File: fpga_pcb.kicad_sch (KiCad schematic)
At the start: 0 parts

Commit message: Aded power and USB
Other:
- added sheet FPGA (FPGA.kicad_sch)
- added sheet Power (Power.kicad_sch)
- added sheet USB (USB.kicad_sch)
- note added: "TLV320ADC6140"
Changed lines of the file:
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@@
 	(generator_version "10.0")
 	(paper "A4")
+	(text "TLV320ADC6140"
+		(exclude_from_sim no)
+		(at 73.152 29.21 0)
+		(effects
+			(font
+				(size 1.27 1.27)
+			)
+		)
+	)
+	(sheet
+		(at 45.72 86.36)
+		(size 43.18 53.34)
+		(exclude_from_sim no)
+		(in_bom yes)
+		(on_board yes)
+		(dnp no)
+		(fields_autoplaced yes)
+		(stroke
+			(width 0.1524)
+			(type solid)
+		)
+		(fill
+			(color 0 0 0 0)
+		)
+		(property "Sheetname" "USB"
+			(at 45.72 85.6484 0)
+			(show_name no)
+			(do_not_autoplace no)
+			(effects
+				(font
+					(size 1.27 1.27)
+				)
+				(justify left bottom)
+			)
+		)
+		(property "Sheetfile" "USB.kicad_sch"
+			(at 45.72 140.2846 0)
+			(show_name no)
+			(do_not_autoplace no)
+			(effects
+				(font
+					(size 1.27 1.27)
+				)
+				(justify left top)
+			)
+		)
+		(pin "FTDI_SPI" bidirectional
+			(at 88.9 93.98 0)
+			(effects
+				(font
+					(size 1.27 1.27)
+				)
+				(justify right)
+			)
+		)
+		(pin "FTDI_BB" bidirectional
+			(at 88.9 105.41 0)
+			(effects
+				(font
+					(size 1.27 1.27)
+				)
+				(justify right)
+			)
+		)
+		(pin "FTDI_JTAG" bidirectional
+			(at 88.9 97.79 0)
+			(effects
+				(font
+					(size 1.27 1.27)
+				)
+				(justify right)
+			)
+		)
+		(pin "FTDI_UART" bidirectional
+			(at 88.9 101.6 0)
+			(effects
+				(font
+					(size 1.27 1.27)
+				)
+				(justify right)
+			)
+		)
+		(instances
+			(project "fpga_pcb"
+				(path "/0e44f7b0-1a4a-4ef8-a122-38b9269be26a"
+					(page "4")
+				)
+			)
+		)
+	)
+	(sheet
+		(at 121.92 85.09)
+		(size 49.53 50.8)
+		(exclude_from_sim no)
+		(in_bom yes)
+		(on_board yes)
+		(dnp no)
+		(fields_autoplaced yes)
+		(stroke
+			(width 0.1524)
+			(type solid)
+		)
+		(fill
+			(color 0 0 0 0)
+		)
+		(property "Sheetname" "FPGA"
+			(at 121.92 84.3784 0)
+			(show_name no)
+			(do_not_autoplace no)
+			(effects
+				(font
+					(size 1.27 1.27)
+				)
+				(justify left bottom)
+			)
+		)
+		(property "Sheetfile" "FPGA.kicad_sch"
+			(at 121.92 136.4746 0)
+			(show_name no)
+			(do_not_autoplace no)
+			(effects
+				(font
+					(size 1.27 1.27)
+				)
+				(justify left top)
+			)
+		)
+		(pin "FTDI_JTAG" bidirectional
+			(at 121.92 104.14 180)
+			(effects
+				(font
+					(size 1.27 1.27)
+				)
+				(justify left)
+			)
+		)
+		(pin "FTDI_SPI" bidirectional
+			(at 121.92 100.33 180)
+			(effects
+				(font
+					(size 1.27 1.27)
+				)
+				(justify left)
+			)
+		)
+		(instances
+			(project "fpga_pcb"
+				(path "/0e44f7b0-1a4a-4ef8-a122-38b9269be26a"
+					(page "2")
+				)
+			)
+		)
+	)
+	(sheet
+		(at 233.68 17.78)
+		(size 33.02 40.64)
+		(exclude_from_sim no)
+		(in_bom yes)
+		(on_board yes)
+		(dnp no)
+		(fields_autoplaced yes)
+		(stroke
+			(width 0.1524)
+			(type solid)
+		)
+		(fill
+			(color 0 0 0 0)
+		)
+		(property "Sheetname" "Power"
+			(at 233.68 17.0684 0)
+			(show_name no)
+			(do_not_autoplace no)
+			(effects
+				(font
+					(size 1.27 1.27)
+				)
+				(justify left bottom)
+			)
+		)
+		(property "Sheetfile" "Power.kicad_sch"
+			(at 233.68 59.0046 0)
+			(show_name no)
+			(do_not_autoplace no)
+			(effects
+				(font
+					(size 1.27 1.27)
+				)
+				(justify left top)
+			)
+		)
+		(instances
+			(project "fpga_pcb"
+				(path "/0e44f7b0-1a4a-4ef8-a122-38b9269be26a"
+					(page "3")
+				)
+			)
+		)
+	)
 	(sheet_instances
 		(path "/"

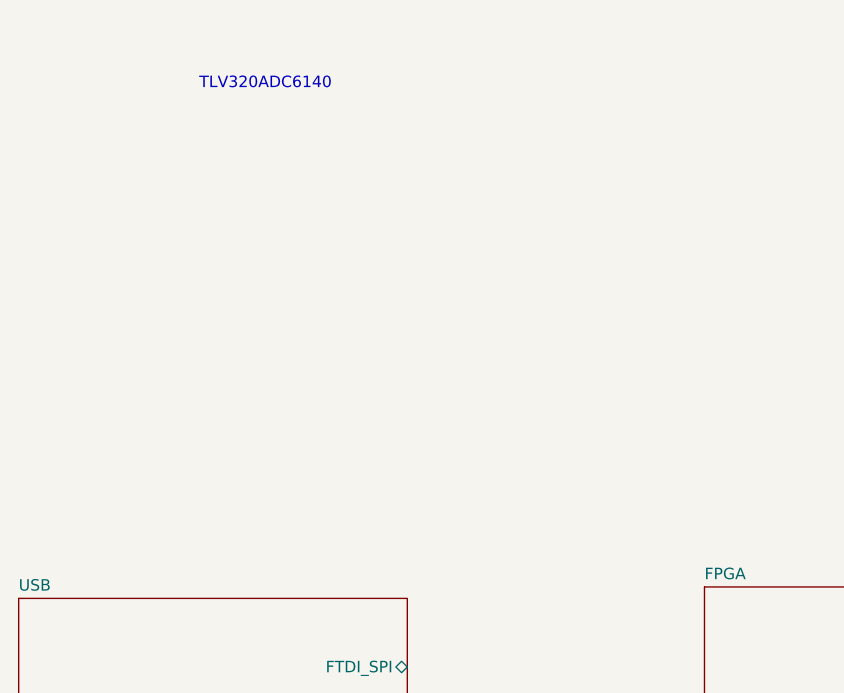
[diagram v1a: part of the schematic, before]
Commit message: Added ADC
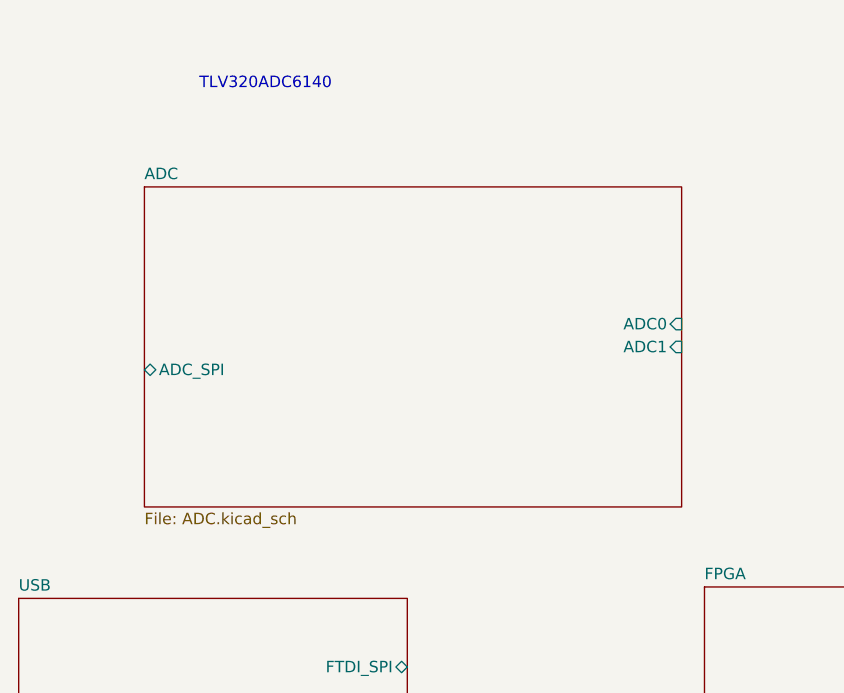
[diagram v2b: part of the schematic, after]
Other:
- added sheet ADC (ADC.kicad_sch)
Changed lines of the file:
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@@
+	)
+	(sheet
+		(at 59.69 40.64)
+		(size 59.69 35.56)
+		(exclude_from_sim no)
+		(in_bom yes)
+		(on_board yes)
+		(dnp no)
+		(fields_autoplaced yes)
+		(stroke
+			(width 0.1524)
+			(type solid)
+		)
+		(fill
+			(color 0 0 0 0)
+		)
+		(property "Sheetname" "ADC"
+			(at 59.69 39.9284 0)
+			(show_name no)
+			(do_not_autoplace no)
+			(effects
+				(font
+					(size 1.27 1.27)
+				)
+				(justify left bottom)
+			)
+		)
+		(property "Sheetfile" "ADC.kicad_sch"
+			(at 59.69 76.7846 0)
+			(show_name no)
+			(do_not_autoplace no)
+			(effects
+				(font
+					(size 1.27 1.27)
+				)
+				(justify left top)
+			)
+		)
+		(pin "ADC0" input
+			(at 119.38 55.88 0)
+			(effects
+				(font
+					(size 1.27 1.27)
+				)
+				(justify right)
+			)
+		)
+		(pin "ADC1" input
+			(at 119.38 58.42 0)
+			(effects
+				(font
+					(size 1.27 1.27)
+				)
+				(justify right)
+			)
+		)
+		(pin "ADC_SPI" bidirectional
+			(at 59.69 60.96 180)
+			(effects
+				(font
+					(size 1.27 1.27)
+				)
+				(justify left)
+			)
+		)
+		(instances
+			(project "fpga_pcb"
+				(path "/0e44f7b0-1a4a-4ef8-a122-38b9269be26a"
+					(page "5")
+				)
+			)
+		)
 	)
 	(sheet

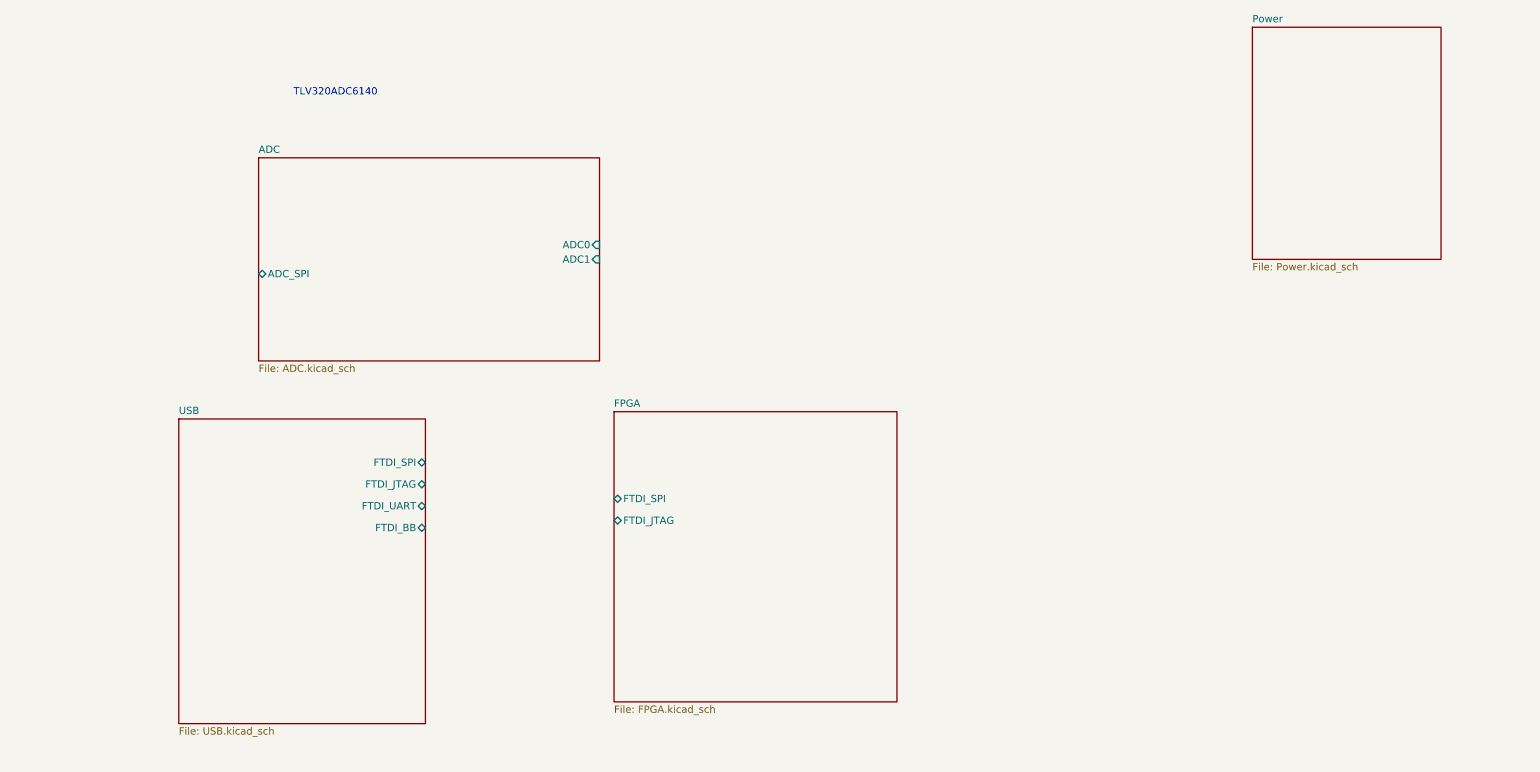
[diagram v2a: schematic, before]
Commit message: Added SRAM and removed old ADC
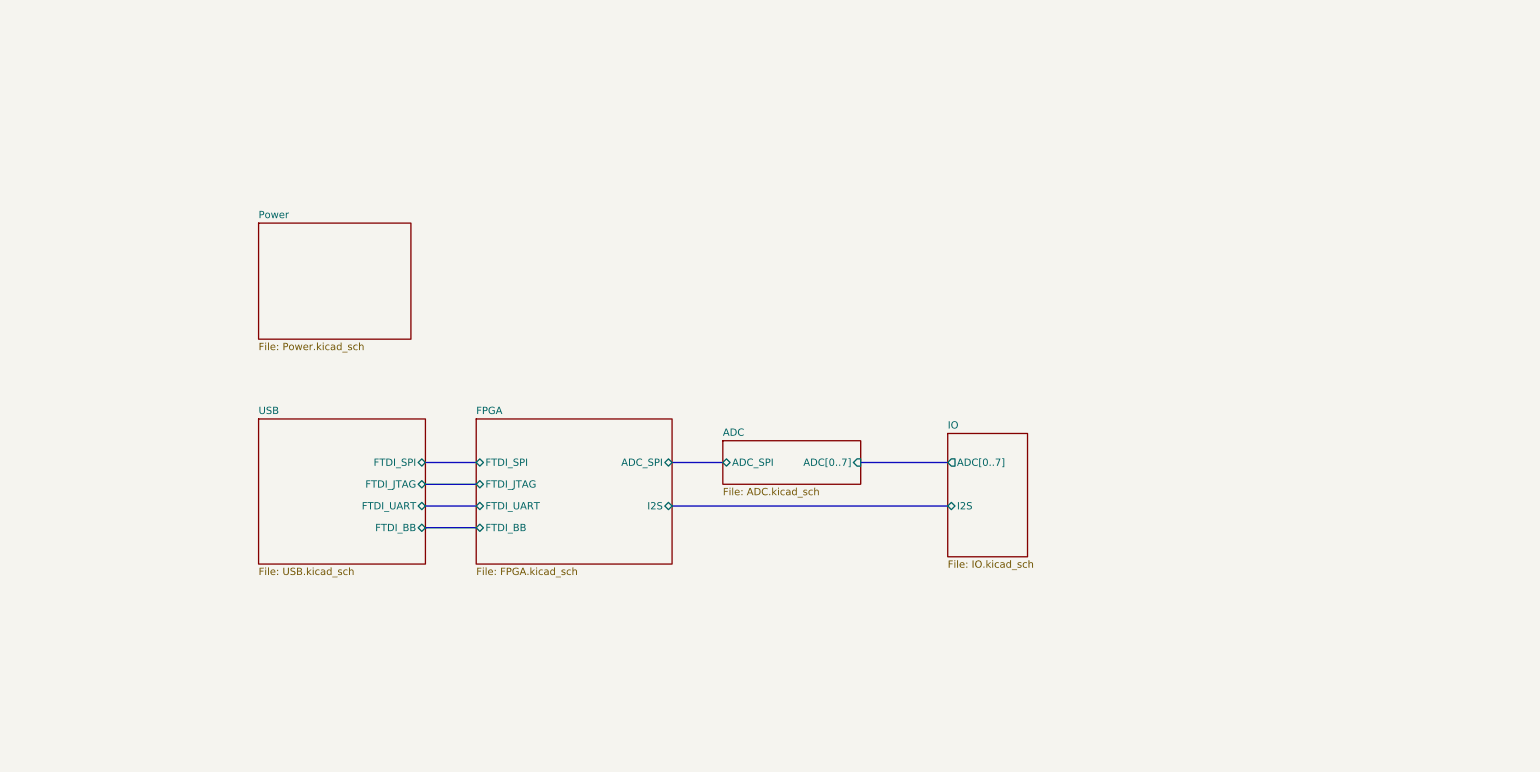
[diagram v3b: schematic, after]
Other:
- added sheet IO (IO.kicad_sch)
- sheet ADC ports: added ADC[0..7]; removed ADC0, ADC1
- sheet FPGA ports: added ADC_SPI, FTDI_BB, FTDI_UART, I2S; removed none
- note removed: "TLV320ADC6140"
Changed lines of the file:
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@@
 	(generator_version "10.0")
 	(paper "A4")
-	(text "TLV320ADC6140"
-		(exclude_from_sim no)
-		(at 73.152 29.21 0)
-		(effects
-			(font
-				(size 1.27 1.27)
-			)
+	(bus
+		(pts
+			(xy 88.9 101.6) (xy 97.79 101.6)
+		)
+		(stroke
+			(width 0)
+			(type default)
+		)
+	)
+	(bus
+		(pts
+			(xy 88.9 105.41) (xy 97.79 105.41)
+		)
+		(stroke
+			(width 0)
+			(type default)
+		)
+	)
+	(bus
+		(pts
+			(xy 88.9 97.79) (xy 97.79 97.79)
+		)
+		(stroke
+			(width 0)
+			(type default)
+		)
+	)
+	(bus
+		(pts
+			(xy 132.08 93.98) (xy 140.97 93.98)
+		)
+		(stroke
+			(width 0)
+			(type default)
+		)
+	)
+	(bus
+		(pts
+			(xy 132.08 101.6) (xy 180.34 101.6)
+		)
+		(stroke
+			(width 0)
+			(type default)
+		)
+	)
+	(bus
+		(pts
+			(xy 165.1 93.98) (xy 180.34 93.98)
+		)
+		(stroke
+			(width 0)
+			(type default)
+		)
+	)
+	(bus
+		(pts
+			(xy 88.9 93.98) (xy 97.79 93.98)
+		)
+		(stroke
+			(width 0)
+			(type default)
 		)
 	)
 	(sheet
-		(at 45.72 86.36)
-		(size 43.18 53.34)
+		(at 59.69 86.36)
+		(size 29.21 25.4)
 		(exclude_from_sim no)
 		(in_bom yes)
@@
 		)
 		(property "Sheetname" "USB"
-			(at 45.72 85.6484 0)
+			(at 59.69 85.6484 0)
 			(show_name no)
 			(do_not_autoplace no)
@@
 		)
 		(property "Sheetfile" "USB.kicad_sch"
-			(at 45.72 140.2846 0)
+			(at 59.69 112.3446 0)
 			(show_name no)
 			(do_not_autoplace no)
@@
 	)
 	(sheet
-		(at 121.92 85.09)
-		(size 49.53 50.8)
+		(at 97.79 86.36)
+		(size 34.29 25.4)
 		(exclude_from_sim no)
 		(in_bom yes)
@@
 		)
 		(property "Sheetname" "FPGA"
-			(at 121.92 84.3784 0)
+			(at 97.79 85.6484 0)
 			(show_name no)
 			(do_not_autoplace no)
@@
 		)
 		(property "Sheetfile" "FPGA.kicad_sch"
-			(at 121.92 136.4746 0)
+			(at 97.79 112.3446 0)
 			(show_name no)
 			(do_not_autoplace no)
@@
 		)
 		(pin "FTDI_JTAG" bidirectional
-			(at 121.92 104.14 180)
+			(at 97.79 97.79 180)
 			(effects
 				(font
@@
 		)
 		(pin "FTDI_SPI" bidirectional
-			(at 121.92 100.33 180)
-			(effects
-				(font
-					(size 1.27 1.27)
-				)
-				(justify left)
+			(at 97.79 93.98 180)
+			(effects
+				(font
+					(size 1.27 1.27)
+				)
+				(justify left)
+			)
+		)
+		(pin "ADC_SPI" bidirectional
+			(at 132.08 93.98 0)
+			(effects
+				(font
+					(size 1.27 1.27)
+				)
+				(justify right)
+			)
+		)
+		(pin "FTDI_BB" bidirectional
+			(at 97.79 105.41 180)
+			(effects
+				(font
+					(size 1.27 1.27)
+				)
+				(justify left)
+			)
+		)
+		(pin "FTDI_UART" bidirectional
+			(at 97.79 101.6 180)
+			(effects
+				(font
+					(size 1.27 1.27)
+				)
+				(justify left)
+			)
+		)
+		(pin "I2S" bidirectional
+			(at 132.08 101.6 0)
+			(effects
+				(font
+					(size 1.27 1.27)
+				)
+				(justify right)
 			)
 		)
@@
 	)
 	(sheet
-		(at 59.69 40.64)
-		(size 59.69 35.56)
+		(at 140.97 90.17)
+		(size 24.13 7.62)
 		(exclude_from_sim no)
 		(in_bom yes)
@@
 		)
 		(property "Sheetname" "ADC"
-			(at 59.69 39.9284 0)
+			(at 140.97 89.4584 0)
 			(show_name no)
 			(do_not_autoplace no)
@@
 		)
 		(property "Sheetfile" "ADC.kicad_sch"
-			(at 59.69 76.7846 0)
+			(at 140.97 98.3746 0)
 			(show_name no)
 			(do_not_autoplace no)
@@
 			)
 		)
-		(pin "ADC0" input
-			(at 119.38 55.88 0)
-			(effects
-				(font
-					(size 1.27 1.27)
-				)
-				(justify right)
-			)
-		)
-		(pin "ADC1" input
-			(at 119.38 58.42 0)
-			(effects
-				(font
-					(size 1.27 1.27)
-				)
-				(justify right)
-			)
-		)
 		(pin "ADC_SPI" bidirectional
-			(at 59.69 60.96 180)
-			(effects
-				(font
-					(size 1.27 1.27)
-				)
-				(justify left)
+			(at 140.97 93.98 180)
+			(effects
+				(font
+					(size 1.27 1.27)
+				)
+				(justify left)
+			)
+		)
+		(pin "ADC[0..7]" input
+			(at 165.1 93.98 0)
+			(effects
+				(font
+					(size 1.27 1.27)
+				)
+				(justify right)
 			)
 		)
@@
 			(project "fpga_pcb"
 				(path "/0e44f7b0-1a4a-4ef8-a122-38b9269be26a"
-					(page "5")
+					(page "6")
 				)
 			)
@@
 	)
 	(sheet
-		(at 233.68 17.78)
-		(size 33.02 40.64)
+		(at 180.34 88.9)
+		(size 13.97 21.59)
 		(exclude_from_sim no)
 		(in_bom yes)
@@
 			(color 0 0 0 0)
 		)
+		(property "Sheetname" "IO"
+			(at 180.34 88.1884 0)
+			(show_name no)
+			(do_not_autoplace no)
+			(effects
+				(font
+					(size 1.27 1.27)
+				)
+				(justify left bottom)
+			)
+		)
+		(property "Sheetfile" "IO.kicad_sch"
+			(at 180.34 111.0746 0)
+			(show_name no)
+			(do_not_autoplace no)
+			(effects
+				(font
+					(size 1.27 1.27)
+				)
+				(justify left top)
+			)
+		)
+		(pin "I2S" bidirectional
+			(at 180.34 101.6 180)
+			(effects
+				(font
+					(size 1.27 1.27)
+				)
+				(justify left)
+			)
+		)
+		(pin "ADC[0..7]" output
+			(at 180.34 93.98 180)
+			(effects
+				(font
+					(size 1.27 1.27)
+				)
+				(justify left)
+			)
+		)
+		(instances
+			(project "fpga_pcb"
+				(path "/0e44f7b0-1a4a-4ef8-a122-38b9269be26a"
+					(page "5")
+				)
+			)
+		)
+	)
+	(sheet
+		(at 59.69 52.07)
+		(size 26.67 20.32)
+		(exclude_from_sim no)
+		(in_bom yes)
+		(on_board yes)
+		(dnp no)
+		(fields_autoplaced yes)
+		(stroke
+			(width 0.1524)
+			(type solid)
+		)
+		(fill
+			(color 0 0 0 0)
+		)
 		(property "Sheetname" "Power"
-			(at 233.68 17.0684 0)
+			(at 59.69 51.3584 0)
 			(show_name no)
 			(do_not_autoplace no)
@@
 		)
 		(property "Sheetfile" "Power.kicad_sch"
-			(at 233.68 59.0046 0)
-			(show_name no)
-			(do_not_autoplace no)
+			(at 59.69 72.9746 0)
+			(show_name no)
+			(do_not_autoplace no)

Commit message: Initial design
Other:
- sheet ADC ports: added ADC_SPI{CS SCLK DIN DOUT}; removed ADC_SPI
- sheet FPGA ports: added ADC_SPI{CS SCLK DIN DOUT}, BB[0..7], FT{SCLK MOSI MISO CS RESETN HOLD}, I2S{SCK WS DATA[0..3]}, JTAG{TCK TDI TDO TMS}, UART{TX RX}; removed ADC_SPI, FTDI_BB, FTDI_JTAG, FTDI_SPI, FTDI_UART, I2S
- sheet IO ports: added FT{SCLK MOSI MISO CS RESETN HOLD}, I2S{SCK DATA[0..3] WS}, JTAG{TCK TDI TDO TMS}, UART{TX RX}; removed I2S
- sheet USB ports: added BB[0..7], FT{SCLK MOSI MISO CS RESETN HOLD}, JTAG{TCK TDI TDO TMS}, UART{TX RX}; removed FTDI_BB, FTDI_JTAG, FTDI_SPI, FTDI_UART
